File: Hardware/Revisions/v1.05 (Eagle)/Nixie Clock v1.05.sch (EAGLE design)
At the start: 89 parts, among them J2 ISCP, J5 HRO_TYPE-C-31-M-12, T1 PZTA92, T2 PZTA42, T3 CSD18543Q3A, U1 ATMEGA2560AU, U10 MIC5504-3.3YM5TR, U11 L80, U12 IP2721, U13 LM340MP-05, U14 LM340MP-05, U2 CH340C, U7 NCH8200HV, U8 DS3231SN#T&R, U9 MIC5504-3.3YM5TR, X1 CSTCR6M00G53Z

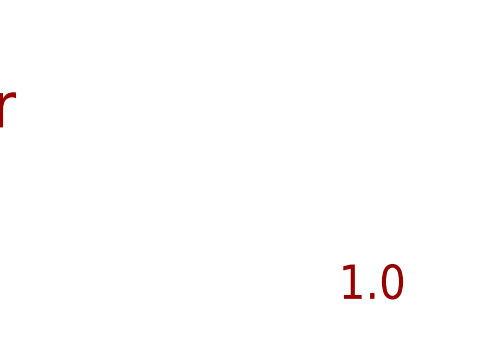
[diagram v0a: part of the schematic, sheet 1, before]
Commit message: rearranged the hardware file structure and added the KiCad files
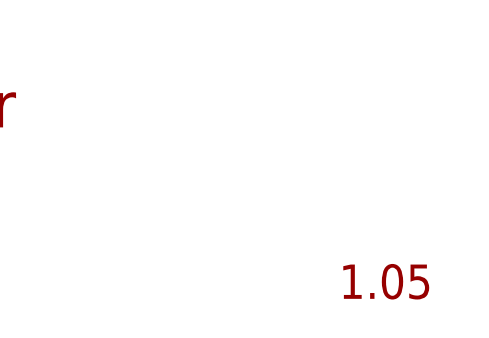
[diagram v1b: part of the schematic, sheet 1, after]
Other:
- note added: "1.05"
- note removed: "1.0"
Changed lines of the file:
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@@
 <plain>
 <text x="48.26" y="-109.22" size="5.08" layer="94">Miccrocontroller</text>
-<text x="134.62" y="-128.27" size="3.81" layer="94">1.0</text>
+<text x="134.62" y="-128.27" size="3.81" layer="94">1.05</text>
 </plain>
 <instances>
@@
 <text x="-91.44" y="157.48" size="3.81" layer="91">USB to Serial</text>
 <text x="175.26" y="-45.72" size="5.08" layer="94">Comunication</text>
-<text x="261.62" y="-64.77" size="3.81" layer="94">1.0</text>
+<text x="261.62" y="-64.77" size="3.81" layer="94">1.05</text>
 <text x="43.18" y="157.48" size="3.81" layer="91">ISCP</text>
 <text x="129.54" y="157.48" size="3.81" layer="91">Serial header</text>
@@
 <text x="-50.8" y="139.7" size="3.81" layer="91">3.3V</text>
 <text x="109.22" y="-93.98" size="5.08" layer="94">Power</text>
-<text x="195.58" y="-113.03" size="3.81" layer="94">1.0</text>
+<text x="195.58" y="-113.03" size="3.81" layer="94">1.05</text>
 <text x="-182.88" y="55.88" size="3.81" layer="91">USB PD</text>
 <text x="-190.5" y="139.7" size="3.81" layer="91">5V</text>
@@
 <text x="50.8" y="152.4" size="3.81" layer="91">GPS</text>
 <text x="175.26" y="-63.5" size="5.08" layer="94">RTC and GPS</text>
-<text x="261.62" y="-82.55" size="3.81" layer="94">1.0</text>
+<text x="261.62" y="-82.55" size="3.81" layer="94">1.05</text>
 <text x="-58.42" y="71.12" size="3.81" layer="91">Settings</text>
 <text x="60.96" y="68.58" size="3.81" layer="91">Photoresistor</text>
@@
 <text x="22.86" y="73.66" size="3.81" layer="91">Nixie and Drivers</text>
 <text x="281.94" y="-93.98" size="5.08" layer="94">Nixie Tubes and Drivers</text>
-<text x="368.3" y="-113.03" size="3.81" layer="94">1.0</text>
+<text x="368.3" y="-113.03" size="3.81" layer="94">1.05</text>
 <text x="205.74" y="-12.7" size="2.54" layer="91">colon</text>
 </plain>
